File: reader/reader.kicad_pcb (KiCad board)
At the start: 2 copper layers, 70 parts, among them J1 USB_B_Mini, J2 swd, J3 Conn_01x06, J4 v_sup, SW1 SW_Push, U1 BA33BC0FP-E2, U2 ST25R95, U3 STM32G051GxU, U4 FC2004C03-NSWBBW-91*E, Y1 27.12MHz, Y2 ABLS-24.000MHZ-20-B-3-H-T

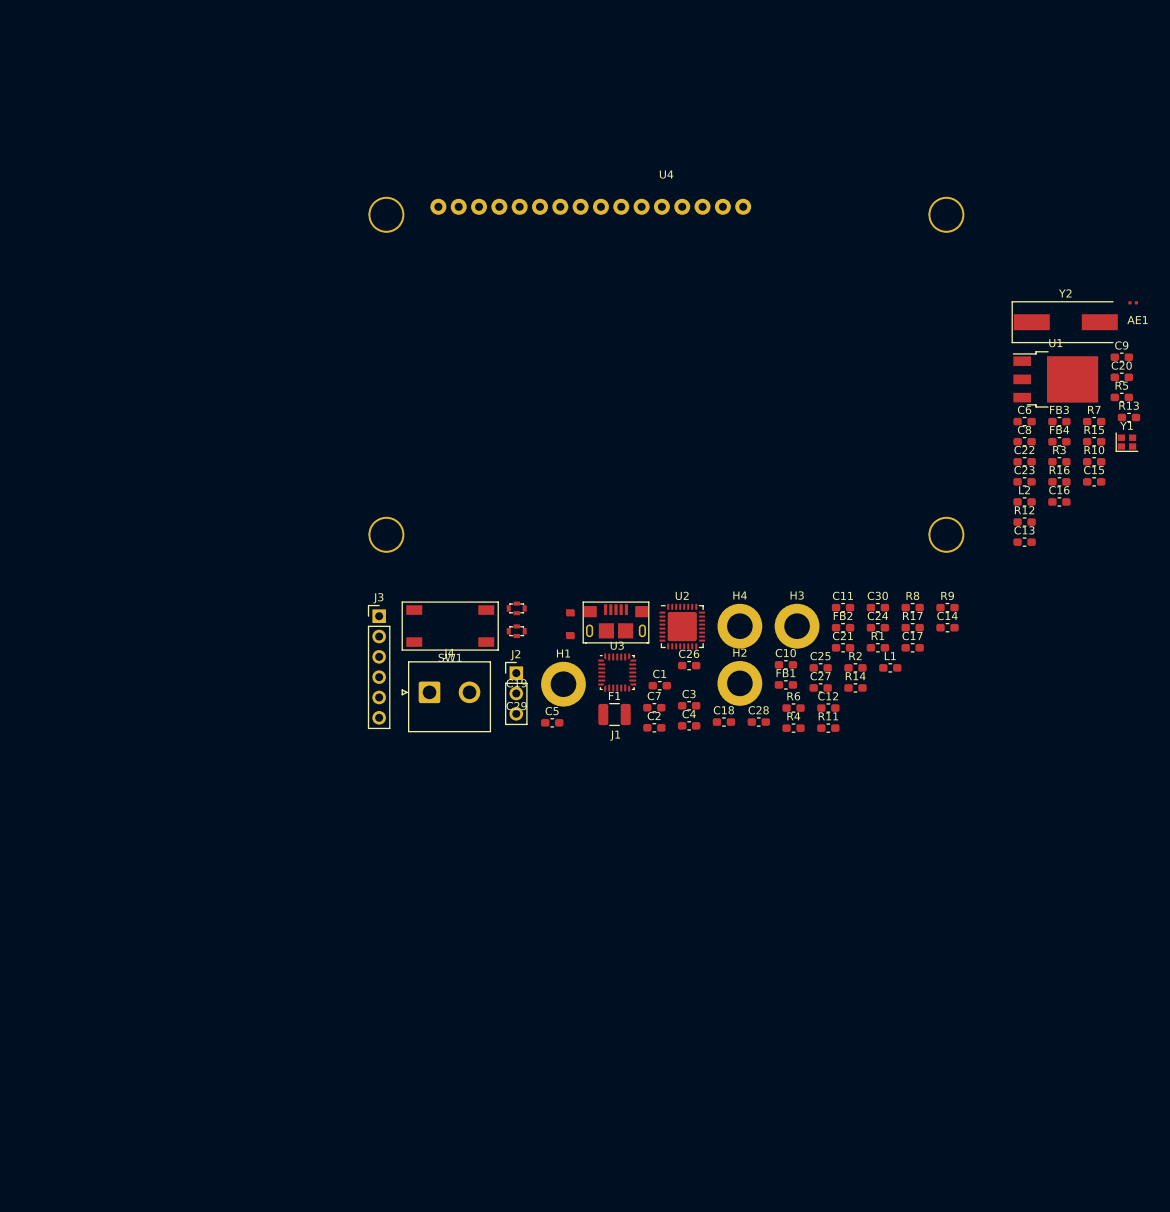
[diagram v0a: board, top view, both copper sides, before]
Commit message: Some placement and antenna
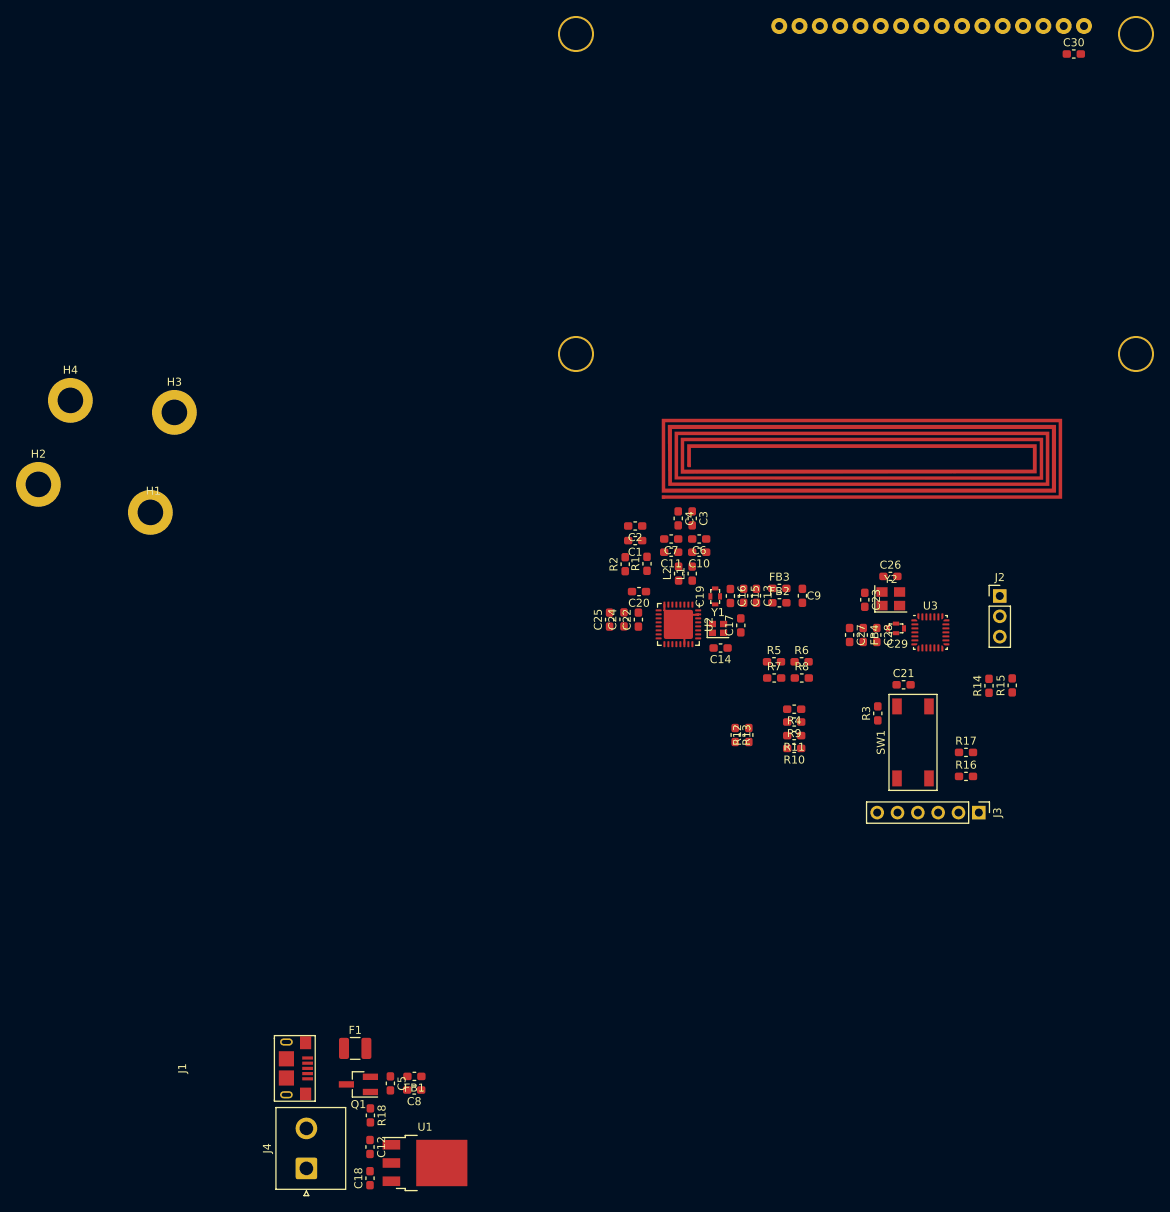
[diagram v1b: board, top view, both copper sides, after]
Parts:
- added Q1: CPH3350-TL-W, Package_TO_SOT_SMD:SOT-23_Handsoldering, F.Cu at (89.5, 165.2)
- added R18: 10k, Resistor_SMD:R_0603_1608Metric_Pad1.05x0.95mm_HandSolder, F.Cu at (91.0, 169.1)
- AE1: footprint good_things:rfid_antenna -> good_things:antenna_04p_04w_5turn
- C23, C26: value 33pF -> 16p
- U4: moved to B.Cu
- Y2: value ABLS-24.000MHZ-20-B-3-H-T -> MCSJK-7U-27.00-12-10-60-B-10; footprint Crystal:Crystal_SMD_HC49-SD -> Crystal:Crystal_SMD_Abracon_ABM8G-4Pin_3.2x2.5mm
- moved U1 125.7 mm to (97.8, 175.0)
- moved C8 111.3 mm to (96.5, 165.9), turned to 180 degrees
- moved H2 91.1 mm to (49.5, 90.2)
- moved H4 88.3 mm to (53.5, 79.7)
- moved H3 82.3 mm to (66.5, 81.2)
- moved C12 79.3 mm to (91.0, 173.0), turned to 270 degrees
- moved J3 78.9 mm to (167.1, 131.2), turned to 270 degrees
- moved C30 73.4 mm to (178.9, 36.4)
- moved C18 72.2 mm to (91.0, 176.9), turned to 90 degrees
- moved J1 68.5 mm to (80.5, 163.2), turned to 270 degrees
- moved FB1 67.5 mm to (96.5, 164.2), turned to 180 degrees
- moved C20 66.0 mm to (124.6, 103.6), turned to 180 degrees
- moved R13 63.2 mm to (136.6, 121.5), turned to 270 degrees
- moved J4 61.5 mm to (83.0, 175.7), turned to 90 degrees
- moved J2 61.2 mm to (169.7, 104.2)
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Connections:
- net Net-(C13-Pad1) renamed /5v_filter
- net Net-(C19-Pad3) renamed /5v_rf
- net Net-(C28-Pad1) renamed /mcu_vcc_t
- net Net-(C29-Pad3) renamed /mcu_vcc
- net Net-(J3-Pad2) renamed /i2c_scl_t
- net Net-(J3-Pad3) renamed /i2c_sda_t
- C5 pad 1: /v_fused -> /v_potected
- FB1 pad 2: /v_fused -> /v_potected
- Y1 pad 2: (no net) -> GND
- Y1 pad 4: (no net) -> GND
- Y2 pad 1: /xtal_out -> /xtal_in
- Y2 pad 2: /xtal_in -> GND
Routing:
- net GND: track 0.00 -> 8.99 mm
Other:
- net class antenna added: clearance 0.4, trace_width 0.4, via_dia 0.8, via_drill 0.4

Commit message: Pcb read done
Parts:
- removed H1, H2, H3, H4: MountingHole_Pad, MountingHole:MountingHole_3.2mm_M3_DIN965_Pad
- AE1: footprint good_things:antenna_04p_04w_5turn -> good_things:antenna_1m_07mm_3turn; moved to B.Cu
- J3: value Conn_01x06 -> Conn_01x05; footprint Connector_PinHeader_2.54mm:PinHeader_1x06_P2.54mm_Vertical -> Connector_PinHeader_2.54mm:PinHeader_1x05_P2.54mm_Vertical
- moved C30 62.1 mm to (175.6, 98.4)
- moved U4 61.9 mm to (148.3, 115.7)
- moved U1 56.2 mm to (129.4, 128.5)
- moved C12 56.2 mm to (122.5, 126.5)
- moved C18 56.2 mm to (122.5, 130.4)
- moved C8 56.2 mm to (128.0, 119.4)
- moved C5 56.2 mm to (125.0, 118.6)
- moved F1 56.2 mm to (120.6, 114.2)
- moved FB1 56.2 mm to (128.0, 117.7)
- moved J1 56.2 mm to (112.0, 116.7)
- moved Q1 56.2 mm to (121.0, 118.7)
- moved R18 56.2 mm to (122.5, 122.6)
- moved J4 56.2 mm to (114.5, 129.2)
- moved AE1 11.5 mm to (149.0, 76.0)
- moved R4 9.74 mm to (151.3, 111.9)
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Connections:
- net Net-(C14-Pad2) renamed /rfid_xin
- net Net-(C17-Pad2) renamed /rfid_xout
- net Net-(R10-Pad2) renamed /spi_miso_rfid
- net Net-(R11-Pad2) renamed /spi_ss_rfid
- net Net-(R4-Pad2) renamed /spi_clk_rfid
- net Net-(R5-Pad2) renamed /rfid_ss1
- net Net-(R7-Pad2) renamed /rfid_ss0
- net Net-(R9-Pad2) renamed /spi_mosi_rfid
- net encoder_b renamed keypad_int
- J3 pad 5: encoder_a -> GND
- U2 pad 10: (no net) -> GND
- U2 pad 11: (no net) -> GND
- U2 pad 23: (no net) -> GND
- U2 pad 24: (no net) -> GND
- U2 pad 25: (no net) -> GND
- U2 pad 26: (no net) -> GND
- U2 pad 27: (no net) -> GND
- U2 pad 28: (no net) -> GND
- U2 pad 3: (no net) -> GND
- U2 pad 4: (no net) -> GND
- U2 pad 7: (no net) -> GND
- U3 pad 22: encoder_a -> (no net)
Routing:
- net GND: track 8.99 -> 77.4 mm, vias 0 -> 50
- net +3V3: track 0.00 -> 57.9 mm, vias 0 -> 16
- net nfc_irq_in: track 0.00 -> 57.6 mm, vias 0 -> 4
- net nfc_irq_out: track 0.00 -> 53.5 mm, vias 0 -> 4
- net keypad_int: track 0.00 -> 29.8 mm, vias 0 -> 2
- net /spi_mosi_rfid: track 0.00 -> 25.6 mm
- net /nrst: track 0.00 -> 25.1 mm, vias 0 -> 2
- net /spi_clk_rfid: track 0.00 -> 24.4 mm
- net spi_miso: track 0.00 -> 23.9 mm
- net Net-(AE1-Pad2): track 0.00 -> 23.7 mm, vias 0 -> 3
- net spi_nss: track 0.00 -> 23.0 mm
- net /lcd_d7: track 0.00 -> 22.2 mm
- net /vin: track 0.00 -> 22.0 mm
- net lcd_rs: track 0.00 -> 21.4 mm, vias 0 -> 1
- net /spi_miso_rfid: track 0.00 -> 21.3 mm, vias 0 -> 2
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- added copper zone on B.Cu, net +3V3
- added copper zone on F.Cu, net +3V3
- added copper zone on B.Cu, net +5V
- added copper zone on B.Cu, net GND
- added copper zone on F.Cu, net GND
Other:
- board outline added: 77.5 x 80 mm

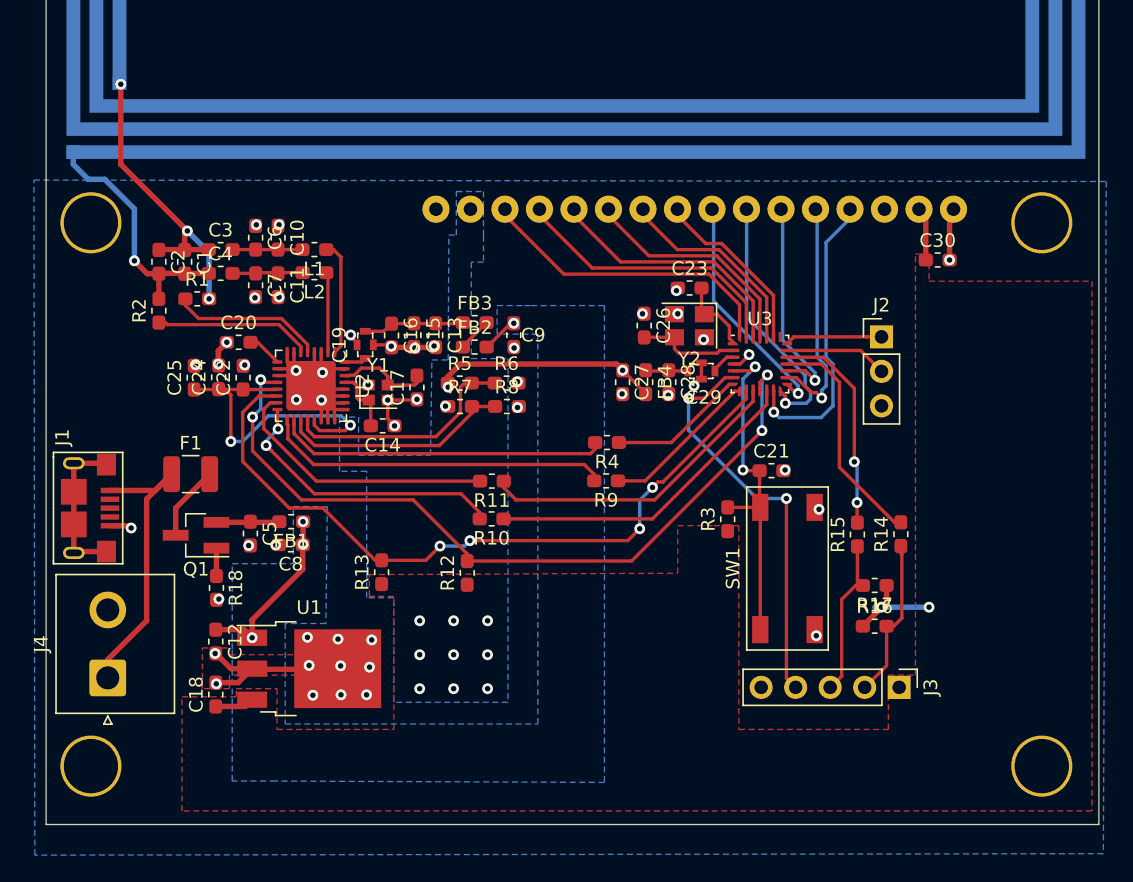
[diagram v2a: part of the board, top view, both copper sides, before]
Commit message: Touchups of main board
start design of keypad
see https://www.thevfdcollective.com/blog/stm32-and-sk6812-rgbw-led
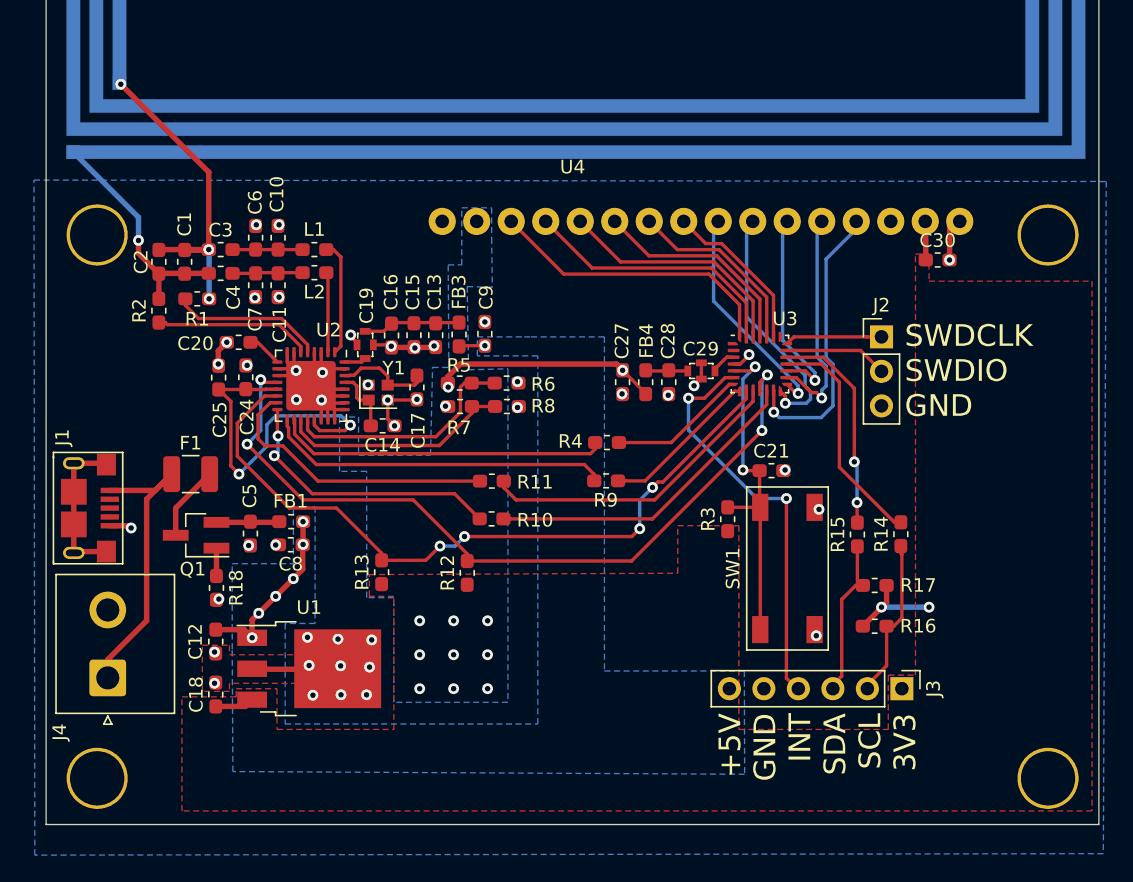
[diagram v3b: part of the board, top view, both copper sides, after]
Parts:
- removed C22: 10n, Capacitor_SMD:C_0603_1608Metric_Pad1.05x0.95mm_HandSolder
- removed C23, C26: 16p, Capacitor_SMD:C_0603_1608Metric_Pad1.05x0.95mm_HandSolder
- removed FB2: 1k@200M, Inductor_SMD:L_0603_1608Metric_Pad1.05x0.95mm_HandSolder
- removed Y2: MCSJK-7U-27.00-12-10-60-B-10, Crystal:Crystal_SMD_Abracon_ABM8G-4Pin_3.2x2.5mm
- J3: value Conn_01x05 -> Conn_01x06; footprint Connector_PinHeader_2.54mm:PinHeader_1x05_P2.54mm_Vertical -> Connector_PinHeader_2.54mm:PinHeader_1x06_P2.54mm_Vertical
- moved C9 2.13 mm to (142.3, 103.9), turned to 90 degrees
- moved C24 2.00 mm to (124.7, 107.1)
- moved C25 1.80 mm to (122.7, 107.1)
- moved FB3 1.45 mm to (140.4, 103.9), turned to 270 degrees
- moved U4 1.01 mm to (148.8, 116.6)
- moved J3 0.22 mm to (173.0, 130.0)
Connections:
- FB3 pad 2: Net-(FB2-Pad1) -> +5V
- J1 pad 2: (no net) -> Net-(J1-Pad2)
- J1 pad 3: (no net) -> Net-(J1-Pad3)
- J1 pad 4: (no net) -> Net-(J1-Pad4)
- U3 pad 1: /xtal_in -> Net-(U3-Pad1)
- U3 pad 2: /xtal_out -> Net-(U3-Pad2)
- U3 pad 22: (no net) -> Net-(U3-Pad22)
- U4 pad 3: (no net) -> Net-(U4-Pad3)
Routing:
- net /xtal_out: track 7.65 -> 0.00 mm
- net GND: track 77.4 -> 71.1 mm, vias 50 -> 45
- net /xtal_in: track 5.61 -> 0.00 mm
- net Net-(FB2-Pad1): track 2.53 -> 0.00 mm
- net +3V3: track 57.9 -> 59.3 mm
- net Net-(AE1-Pad1): track 18.3 -> 17.1 mm
- net /spi_ss_rfid: track 20.1 -> 21.2 mm
- net +5V: track 15.7 -> 14.9 mm, vias 4 -> 7
- net /spi_miso_rfid: track 21.3 -> 20.6 mm
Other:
- board text added: "+5V GND INT SDA SCL 3V3"
- board text added: "GND 5V"
- board text added: "Monopoly reader Anton Lööf 2021 Rev1"
- board text added: "SWDCLK SWDIO GND"

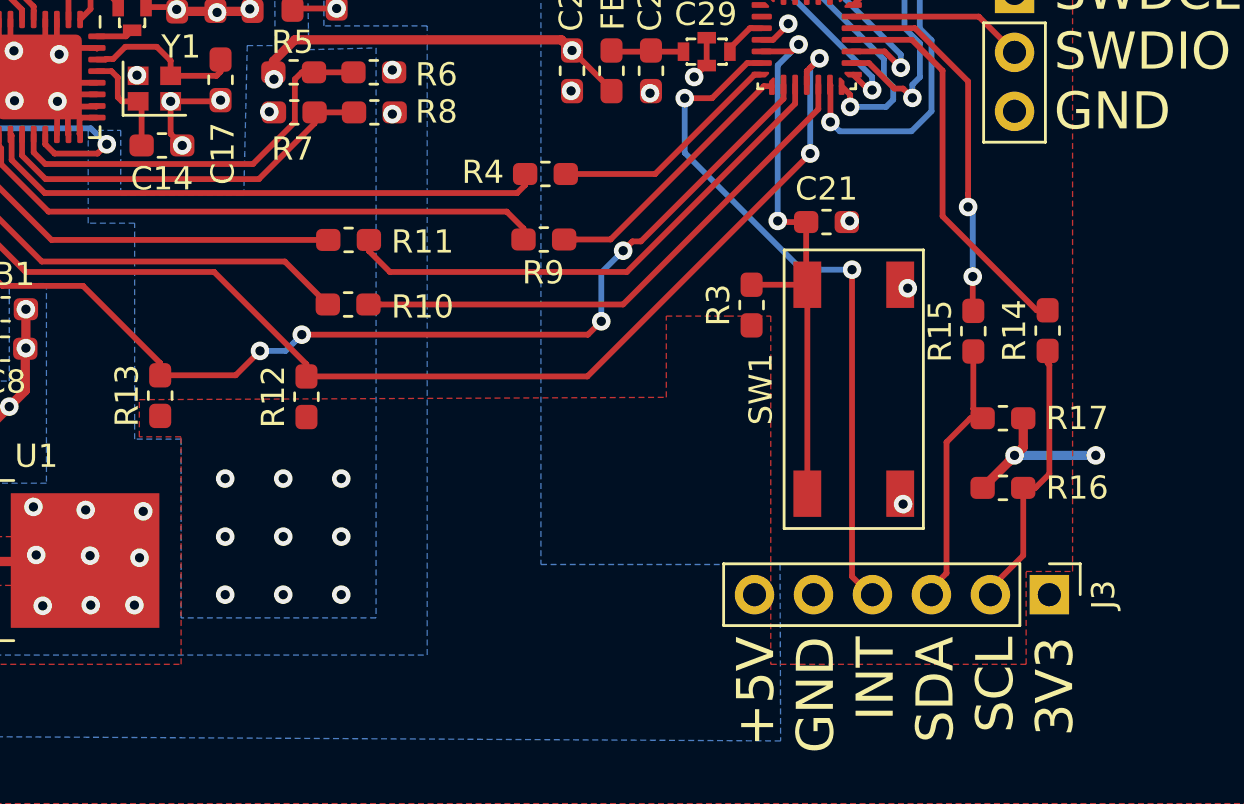
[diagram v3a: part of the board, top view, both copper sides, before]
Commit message: Add keypad
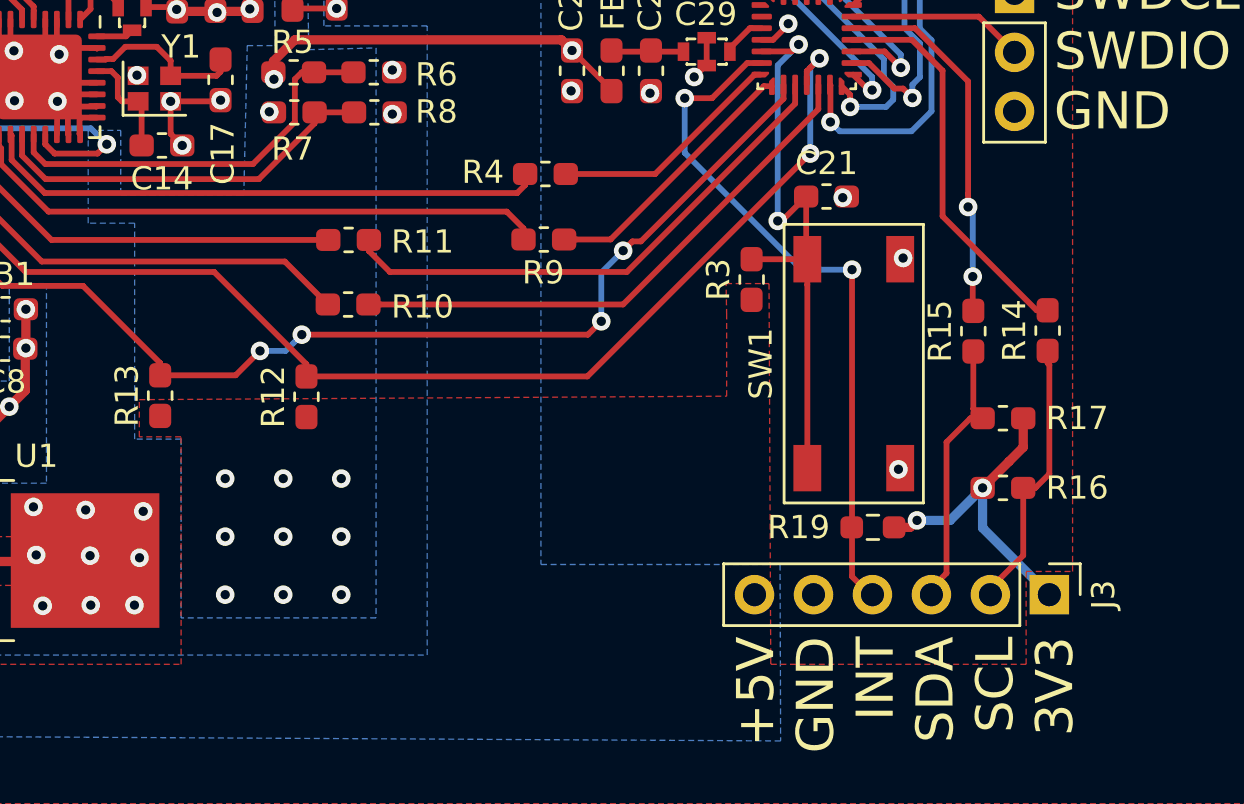
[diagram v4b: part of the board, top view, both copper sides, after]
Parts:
- added R19: 2k2, Resistor_SMD:R_0603_1608Metric_Pad0.98x0.95mm_HandSolder, F.Cu at (165.4, 127.1)
- moved C21 1.10 mm to (163.4, 112.8)
- moved R3 1.10 mm to (160.2, 116.4)
- moved SW1 1.10 mm to (164.6, 120.0)
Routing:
- net +3V3: track 59.3 -> 66.2 mm
